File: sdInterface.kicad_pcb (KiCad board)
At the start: 2 copper layers, 51 x 37 mm, 6 parts, among them J1 SD_Card, J2 Conn_02x12_Counter_Clockwise, U1 MCP1826S

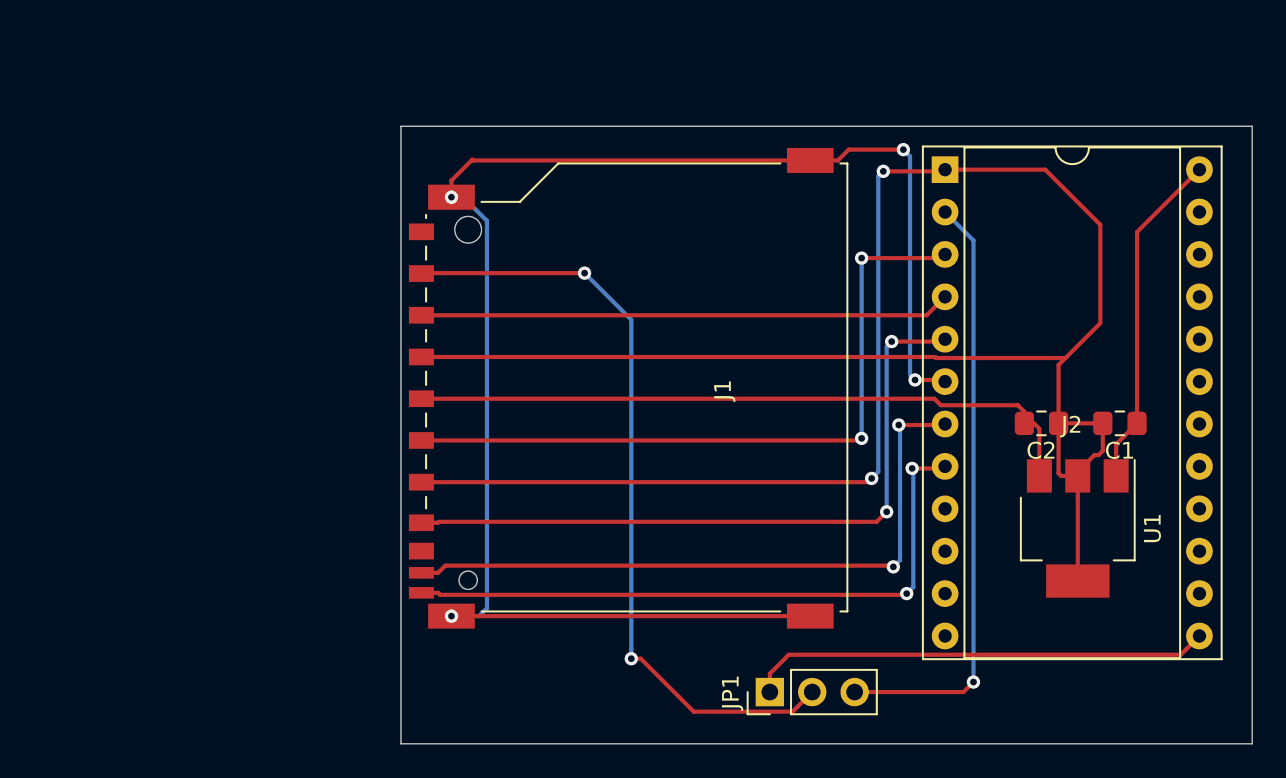
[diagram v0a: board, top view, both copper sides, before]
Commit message: Flipped SD slot 180deg, Added 2mm mounting holes
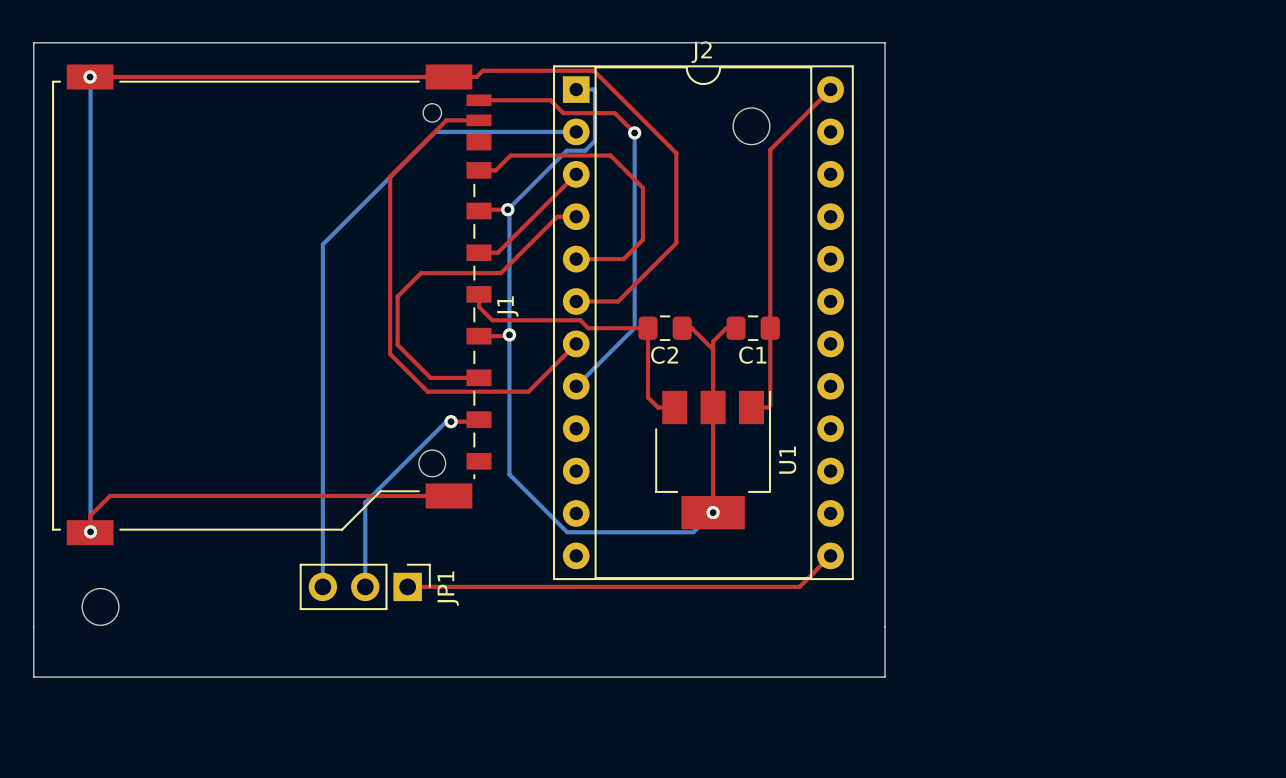
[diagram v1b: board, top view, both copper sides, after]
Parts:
- added REF**: MountingHole_2.2mm_M2, MountingHole:MountingHole_2.2mm_M2, F.Cu at (73.0, 101.8)
- added REF**: MountingHole_2.2mm_M2, MountingHole:MountingHole_2.2mm_M2, F.Cu at (112.0, 73.0)
- moved C2 23.3 mm to (106.8, 85.1)
- moved C1 22.7 mm to (112.1, 85.1)
- moved J2 22.6 mm to (101.5, 70.8)
- moved JP1 22.6 mm to (91.4, 100.6), turned to 270 degrees
- moved U1 22.2 mm to (109.7, 93.0)
- moved J1 21.1 mm to (83.7, 83.7), turned to 270 degrees
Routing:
- net /GND: track 128.8 -> 61.3 mm, vias 2 -> 3
- net Net-(J1-Pad5): track 42.3 -> 7.77 mm, vias 2 -> 0
- net Net-(J1-Pad1): track 46.7 -> 13.9 mm, vias 2 -> 1
- net Net-(C2-Pad2): track 41.0 -> 17.4 mm
- net Net-(J1-Pad7): track 41.7 -> 18.6 mm, vias 2 -> 0
- net Net-(J1-Pad11): track 38.9 -> 26.8 mm, vias 2 -> 1
- net Net-(J1-Pad2): track 31.8 -> 21.3 mm
- net Net-(J1-Pad10): track 40.0 -> 30.6 mm, vias 2 -> 0
- net Net-(J1-Pad12): track 94.6 -> 100.5 mm, vias 4 -> 2
- net Net-(J2-Pad2): track 36.2 -> 38.5 mm, vias 1 -> 0
- net Net-(J2-Pad13): track 27.8 -> 26.1 mm
- net Net-(C1-Pad1): track 20.4 -> 21.6 mm
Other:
- board size 51 x 37 mm -> 51 x 38 mm
